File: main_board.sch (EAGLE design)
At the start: 49 parts, among them IC1 LT1168ACS8, IC2 LT1168ACS8, IC3 LT1168ACS8, IC4 317EMP, U1 TLC272IP, U2 TLC272IP, U3 TLC272IP

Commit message: Progress
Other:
- moved on the sheet: R2
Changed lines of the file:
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@@
 <instance part="SUPPLY10" gate="GND" x="182.88" y="15.24"/>
 <instance part="VDD1" gate="G$1" x="88.9" y="55.88"/>
-<instance part="R2" gate="G$1" x="88.9" y="45.72" rot="R90"/>
+<instance part="R2" gate="G$1" x="88.9" y="48.26" rot="R90"/>
 <instance part="R3" gate="G$1" x="78.74" y="7.62"/>
 <instance part="R10" gate="G$1" x="170.18" y="30.48" rot="R90"/>
@@
 <pinref part="VDD1" gate="G$1" pin="VDD"/>
 <pinref part="R2" gate="G$1" pin="2"/>
-<wire x1="88.9" y1="53.34" x2="88.9" y2="50.8" width="0.1524" layer="91"/>
 </segment>
 <segment>
@@
 <pinref part="R2" gate="G$1" pin="1"/>
 <pinref part="TM2" gate="G$1" pin="A"/>
-<wire x1="88.9" y1="40.64" x2="88.9" y2="38.1" width="0.1524" layer="91"/>
+<wire x1="88.9" y1="43.18" x2="88.9" y2="38.1" width="0.1524" layer="91"/>
 <wire x1="106.68" y1="38.1" x2="88.9" y2="38.1" width="0.1524" layer="91"/>
 <junction x="88.9" y="38.1"/>

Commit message: Merging
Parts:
- removed PAD1, PAD10, PAD11, PAD12, PAD2, PAD25, PAD26, PAD27, PAD28, PAD29, PAD3, PAD30, PAD4, PAD5, PAD6, PAD7, PAD8, PAD9: (no value), wirepad:1,6/0,9
- added C3, C4, C5, C6, C7: 10uF, adafruit:C-USC2012
- added X1, X2, X3: C-GRID-04-70543, con-molex:C-GRID-04-70543
- added X4, X5, X6: C-GRID-02-70543, con-molex:C-GRID-02-70543
- C1: value (none) -> 1uF; device eagle-ltspice:CC2012 -> adafruit:C-USC2012
- C2: value (none) -> 10uF; device eagle-ltspice:CC2012 -> adafruit:C-USC2012
- R13, R7: value (none) -> 30kO
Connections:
- net N$11 renamed U3_1_IN+
- net N$12 renamed IC3_RG1
- net N$13 renamed TM7POT2
- net N$14 renamed IC3_RG8
- net N$15 renamed U3_2_IN+
- net N$2 renamed U1_2IN-
- net N$20 renamed U1_2IN+
- net N$24 renamed U2_2IN-
- net N$25 renamed U2_1IN+
- net N$26 renamed U2_1IN-
- net N$27 renamed TM5POT2
- net N$3 renamed U1_1IN+
- net N$30 renamed U2_2IN+
- net N$4 renamed U1_1IN-
- net N$5 renamed TM2POT2
- net N$6 renamed ADJ
- net N$8 renamed U3_2_IN-
- net N$9 renamed U3_1_IN-
- removed net N$17: IC3.+IN, PAD2.P
- removed net N$18: IC3.-IN, PAD1.P
- removed net N$21: IC1.+IN, PAD26.P
- removed net N$22: IC1.-IN, PAD25.P
- removed net N$31: IC2.+IN, PAD29.P
- removed net N$32: IC2.-IN, PAD28.P
- new net BLUE_IN_B: IC3.+IN, X1-2.S
- new net BLUE_IN_R: IC3.-IN, X1-3.S
- new net GREEN_IN_B: IC1.+IN, X2-2.S
- new net GREEN_IN_R: IC1.-IN, X2-3.S
- new net WHITE_IN_B: IC2.+IN, X3-2.S
- new net WHITE_IN_R: IC2.-IN, X3-3.S
- net GND: now also C3.2, C4.1, C5.1, C6.1, C7.2, X1-4.S, X2-4.S, X3-4.S, X4-2.S, X5-2.S, X6-2.S; no longer PAD10.P, PAD11.P, PAD12.P, PAD7.P, PAD8.P, PAD9.P
- net N$1: now also X4-1.S; no longer PAD27.P
- net N$23: now also X5-1.S; no longer PAD30.P
- net N$7: no longer PAD3.P
- net VCC: now also C4.2, C5.2, C6.2
- net VDD: now also C3.1, C7.1, X1-1.S, X2-1.S, X3-1.S; no longer PAD4.P, PAD5.P, PAD6.P
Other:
- note added: "1. Assign values to all capacitors/resistors, etc... 2. Replace pin headers with MOLEX headers 3. Add capacitor to each output VDD 4. Name your NETS!"
- note removed: "Blue +"
- note removed: "Blue -"
- note removed: "Blue out_B"
- note removed: "Blue out_R"
- note removed: "Green +"
- note removed: "Green -"
- note removed: "Green out_B"
- note removed: "Green out_R"
- note removed: "TransducerGND"
- note removed: "TransducerVDD"
- note removed: "white -"
- note removed: "white+"
- note removed: "white-"
- moved on the sheet: C2, R9

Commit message: Finished board
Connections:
- net N$1 renamed U1_2OUT
- net N$23 renamed U2_2OUT
- net N$7 renamed U3_2OUT
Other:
- moved on the sheet: R12, R2
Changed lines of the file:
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@@
 <instance part="SUPPLY10" gate="GND" x="182.88" y="15.24"/>
 <instance part="VDD1" gate="G$1" x="88.9" y="55.88"/>
-<instance part="R2" gate="G$1" x="88.9" y="48.26" rot="R90"/>
+<instance part="R2" gate="G$1" x="88.9" y="50.8" rot="R90"/>
 <instance part="R3" gate="G$1" x="78.74" y="7.62"/>
 <instance part="R10" gate="G$1" x="170.18" y="30.48" rot="R90"/>
@@
 <instance part="SUPPLY14" gate="GND" x="182.88" y="71.12"/>
 <instance part="VDD2" gate="G$1" x="88.9" y="111.76"/>
-<instance part="R12" gate="G$1" x="88.9" y="101.6" rot="R90"/>
+<instance part="R12" gate="G$1" x="88.9" y="104.14" rot="R90"/>
 <instance part="R13" gate="G$1" x="78.74" y="63.5"/>
 <instance part="R14" gate="G$1" x="170.18" y="86.36" rot="R90"/>
@@
 </segment>
 </net>
-<net name="N$7" class="0">
+<net name="U3_2OUT" class="0">
 <segment>
 <pinref part="R4" gate="G$1" pin="2"/>
@@
 <pinref part="VDD1" gate="G$1" pin="VDD"/>
 <pinref part="R2" gate="G$1" pin="2"/>
+<wire x1="88.9" y1="55.88" x2="88.9" y2="53.34" width="0.1524" layer="91"/>
 </segment>
 <segment>
 <pinref part="VDD2" gate="G$1" pin="VDD"/>
 <pinref part="R12" gate="G$1" pin="2"/>
-<wire x1="88.9" y1="109.22" x2="88.9" y2="106.68" width="0.1524" layer="91"/>
 </segment>
 <segment>
@@
 </segment>
 </net>
-<net name="N$1" class="0">
+<net name="U1_2OUT" class="0">
 <segment>
 <pinref part="R1" gate="G$1" pin="2"/>
@@
 <pinref part="R2" gate="G$1" pin="1"/>
 <pinref part="TM2" gate="G$1" pin="A"/>
-<wire x1="88.9" y1="43.18" x2="88.9" y2="38.1" width="0.1524" layer="91"/>
+<wire x1="88.9" y1="45.72" x2="88.9" y2="38.1" width="0.1524" layer="91"/>
 <wire x1="106.68" y1="38.1" x2="88.9" y2="38.1" width="0.1524" layer="91"/>
 <junction x="88.9" y="38.1"/>
@@
 </segment>
 </net>
-<net name="N$23" class="0">
+<net name="U2_2OUT" class="0">
 <segment>
 <pinref part="R11" gate="G$1" pin="2"/>
@@
 <pinref part="R12" gate="G$1" pin="1"/>
 <pinref part="TM4" gate="G$1" pin="A"/>
-<wire x1="88.9" y1="96.52" x2="88.9" y2="93.98" width="0.1524" layer="91"/>
+<wire x1="88.9" y1="99.06" x2="88.9" y2="93.98" width="0.1524" layer="91"/>
 <wire x1="106.68" y1="93.98" x2="88.9" y2="93.98" width="0.1524" layer="91"/>
 <junction x="88.9" y="93.98"/>

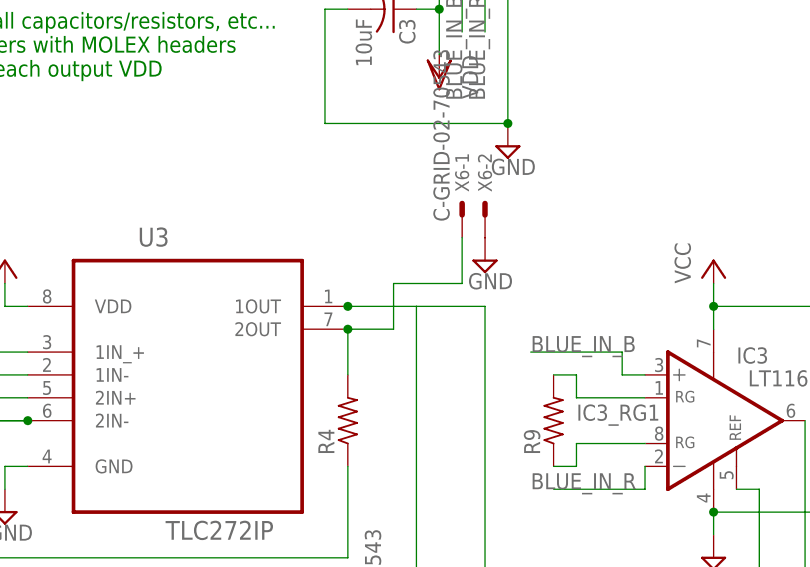
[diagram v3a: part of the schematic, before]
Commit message: Finished board. No errors remaining.
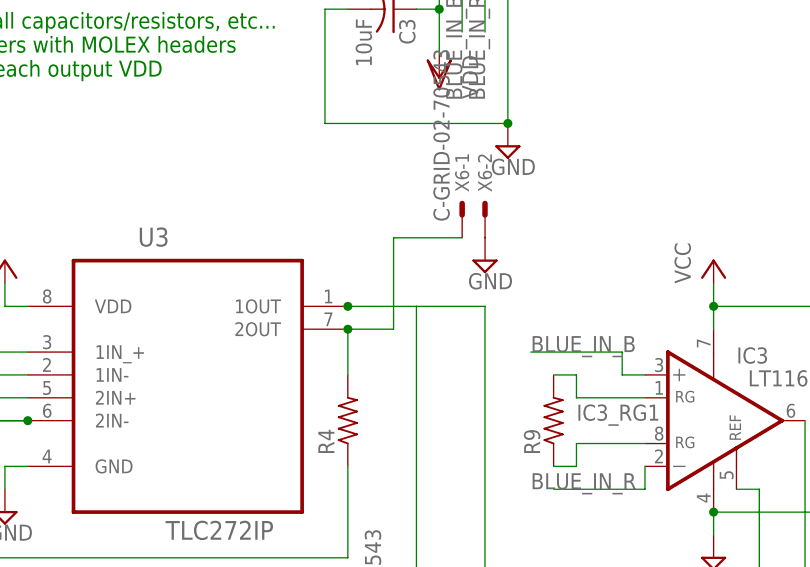
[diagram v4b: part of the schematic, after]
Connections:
- net U3_2OUT: now also X6-1.S
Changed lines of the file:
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@@
 </variantdefs>
 <classes>
-<class number="0" name="default" width="0.3048" drill="0.508">
+<class number="0" name="default" width="0.3048" drill="0.4318">
 <clearance class="0" value="0.254"/>
 </class>
@@
 <pinref part="U3" gate="A" pin="2OUT"/>
 <wire x1="142.24" y1="144.78" x2="142.24" y2="149.86" width="0.1524" layer="91"/>
-<wire x1="142.24" y1="149.86" x2="147.32" y2="149.86" width="0.1524" layer="91"/>
+<pinref part="X6" gate="-1" pin="S"/>
+<wire x1="154.94" y1="160.02" x2="147.32" y2="160.02" width="0.1524" layer="91"/>
+<wire x1="147.32" y1="160.02" x2="147.32" y2="149.86" width="0.1524" layer="91"/>
+<wire x1="147.32" y1="149.86" x2="142.24" y2="149.86" width="0.1524" layer="91"/>
 <junction x="142.24" y="149.86"/>
-<wire x1="147.32" y1="149.86" x2="147.32" y2="154.94" width="0.1524" layer="91"/>
-<wire x1="147.32" y1="154.94" x2="154.94" y2="154.94" width="0.1524" layer="91"/>
-<wire x1="154.94" y1="154.94" x2="154.94" y2="160.02" width="0.1524" layer="91"/>
 </segment>
 </net>

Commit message: Finished.
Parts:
- R1, R4: value (none) -> 10kO
- R10: value (none) -> 110ohm
- R11: value (none) -> 10kO\
- R12, R2: value (none) -> 30kO
- R13: value 30kO -> 2kO
- R14, R9: value (none) -> 110 ohm
- R3, R8: value (none) -> 2kO
- R5: value (none) -> 1KO
- R6: value (none) -> 4kO
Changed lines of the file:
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@@
 <parts>
 <part name="IC3" library="linear-technology" library_urn="urn:adsk.eagle:library:261" deviceset="LT1168" device="S8" technology="AC"/>
-<part name="R4" library="adafruit" deviceset="R-US_" device="R1206"/>
-<part name="R5" library="adafruit" deviceset="R-US_" device="R1206"/>
-<part name="R6" library="adafruit" deviceset="R-US_" device="R1206"/>
+<part name="R4" library="adafruit" deviceset="R-US_" device="R1206" value="10kO"/>
+<part name="R5" library="adafruit" deviceset="R-US_" device="R1206" value="1KO"/>
+<part name="R6" library="adafruit" deviceset="R-US_" device="R1206" value="4kO"/>
 <part name="U3" library="Texas Instruments_By_element14_Batch_1" deviceset="TLC272IP" device=""/>
 <part name="SUPPLY3" library="supply2" library_urn="urn:adsk.eagle:library:372" deviceset="GND" device=""/>
@@
 <part name="TM6" library="adafruit" deviceset="TRIMPOT" device="3386"/>
 <part name="TM7" library="adafruit" deviceset="TRIMPOT" device="3386"/>
-<part name="G1" library="battery" library_urn="urn:adsk.eagle:library:109" deviceset="AB9V" device=""/>
 <part name="P+4" library="supply1" library_urn="urn:adsk.eagle:library:371" deviceset="VCC" device=""/>
 <part name="P+8" library="supply1" library_urn="urn:adsk.eagle:library:371" deviceset="VCC" device=""/>
@@
 <part name="VDD4" library="supply1" library_urn="urn:adsk.eagle:library:371" deviceset="VDD" device=""/>
 <part name="R7" library="adafruit" deviceset="R-US_" device="R1206" value="30kO"/>
-<part name="R8" library="adafruit" deviceset="R-US_" device="R1206"/>
-<part name="R9" library="adafruit" deviceset="R-US_" device="R1206"/>
+<part name="R8" library="adafruit" deviceset="R-US_" device="R1206" value="2kO"/>
+<part name="R9" library="adafruit" deviceset="R-US_" device="R1206" value="110 ohm"/>
 <part name="P+1" library="supply1" library_urn="urn:adsk.eagle:library:371" deviceset="VCC" device=""/>
 <part name="P+2" library="supply1" library_urn="urn:adsk.eagle:library:371" deviceset="VCC" device=""/>
 <part name="IC1" library="linear-technology" library_urn="urn:adsk.eagle:library:261" deviceset="LT1168" device="S8" technology="AC"/>
-<part name="R1" library="adafruit" deviceset="R-US_" device="R1206"/>
+<part name="R1" library="adafruit" deviceset="R-US_" device="R1206" value="10kO"/>
 <part name="U1" library="Texas Instruments_By_element14_Batch_1" deviceset="TLC272IP" device=""/>
 <part name="SUPPLY1" library="supply2" library_urn="urn:adsk.eagle:library:372" deviceset="GND" device=""/>
@@
 <part name="SUPPLY10" library="supply2" library_urn="urn:adsk.eagle:library:372" deviceset="GND" device=""/>
 <part name="VDD1" library="supply1" library_urn="urn:adsk.eagle:library:371" deviceset="VDD" device=""/>
-<part name="R2" library="adafruit" deviceset="R-US_" device="R1206"/>
-<part name="R3" library="adafruit" deviceset="R-US_" device="R1206"/>
-<part name="R10" library="adafruit" deviceset="R-US_" device="R1206"/>
+<part name="R2" library="adafruit" deviceset="R-US_" device="R1206" value="30kO"/>
+<part name="R3" library="adafruit" deviceset="R-US_" device="R1206" value="2kO"/>
+<part name="R10" library="adafruit" deviceset="R-US_" device="R1206" value="110ohm"/>
 <part name="P+3" library="supply1" library_urn="urn:adsk.eagle:library:371" deviceset="VCC" device=""/>
 <part name="P+5" library="supply1" library_urn="urn:adsk.eagle:library:371" deviceset="VCC" device=""/>
 <part name="IC2" library="linear-technology" library_urn="urn:adsk.eagle:library:261" deviceset="LT1168" device="S8" technology="AC"/>
-<part name="R11" library="adafruit" deviceset="R-US_" device="R1206"/>
+<part name="R11" library="adafruit" deviceset="R-US_" device="R1206" value="10kO\"/>
 <part name="U2" library="Texas Instruments_By_element14_Batch_1" deviceset="TLC272IP" device=""/>
 <part name="SUPPLY11" library="supply2" library_urn="urn:adsk.eagle:library:372" deviceset="GND" device=""/>
@@
 <part name="SUPPLY14" library="supply2" library_urn="urn:adsk.eagle:library:372" deviceset="GND" device=""/>
 <part name="VDD2" library="supply1" library_urn="urn:adsk.eagle:library:371" deviceset="VDD" device=""/>
-<part name="R12" library="adafruit" deviceset="R-US_" device="R1206"/>
-<part name="R13" library="adafruit" deviceset="R-US_" device="R1206" value="30kO"/>
-<part name="R14" library="adafruit" deviceset="R-US_" device="R1206"/>
+<part name="R12" library="adafruit" deviceset="R-US_" device="R1206" value="30kO"/>
+<part name="R13" library="adafruit" deviceset="R-US_" device="R1206" value="2kO"/>
+<part name="R14" library="adafruit" deviceset="R-US_" device="R1206" value="110 ohm"/>
 <part name="P+6" library="supply1" library_urn="urn:adsk.eagle:library:371" deviceset="VCC" device=""/>
 <part name="P+7" library="supply1" library_urn="urn:adsk.eagle:library:371" deviceset="VCC" device=""/>
@@
 <part name="SUPPLY16" library="supply2" library_urn="urn:adsk.eagle:library:372" deviceset="GND" device=""/>
 <part name="SUPPLY22" library="supply2" library_urn="urn:adsk.eagle:library:372" deviceset="GND" device=""/>
+<part name="G1" library="battery" deviceset="AB9V" device=""/>
 </parts>
 <sheets>
@@
 <instance part="TM6" gate="G$1" x="83.82" y="147.32" rot="MR270"/>
 <instance part="TM7" gate="G$1" x="83.82" y="124.46" rot="R270"/>
-<instance part="G1" gate="G$1" x="40.64" y="152.4"/>
 <instance part="P+4" gate="VCC" x="58.42" y="157.48"/>
 <instance part="P+8" gate="VCC" x="27.94" y="132.08"/>
@@
 <instance part="SUPPLY16" gate="GND" x="152.4" y="104.14"/>
 <instance part="SUPPLY22" gate="GND" x="152.4" y="48.26"/>
+<instance part="G1" gate="G$1" x="40.64" y="152.4"/>
 </instances>
 <busses>
@@
 </segment>
 <segment>
-<pinref part="G1" gate="G$1" pin="-"/>
 <pinref part="SUPPLY4" gate="GND" pin="GND"/>
 <wire x1="27.94" y1="152.4" x2="22.86" y2="152.4" width="0.1524" layer="91"/>
@@
 <wire x1="38.1" y1="142.24" x2="27.94" y2="142.24" width="0.1524" layer="91"/>
 <wire x1="27.94" y1="142.24" x2="27.94" y2="152.4" width="0.1524" layer="91"/>
+<pinref part="C1" gate="G$1" pin="2"/>
+<pinref part="G1" gate="G$1" pin="-"/>
 <junction x="27.94" y="152.4"/>
-<pinref part="C1" gate="G$1" pin="2"/>
 </segment>
 <segment>
@@
 <net name="VCC" class="0">
 <segment>
-<pinref part="G1" gate="G$1" pin="+"/>
 <pinref part="P+4" gate="VCC" pin="VCC"/>
 <wire x1="53.34" y1="152.4" x2="58.42" y2="152.4" width="0.1524" layer="91"/>
@@
 <wire x1="45.72" y1="142.24" x2="53.34" y2="142.24" width="0.1524" layer="91"/>
 <wire x1="53.34" y1="142.24" x2="53.34" y2="152.4" width="0.1524" layer="91"/>
+<pinref part="C1" gate="G$1" pin="1"/>
+<pinref part="G1" gate="G$1" pin="+"/>
 <junction x="53.34" y="152.4"/>
-<pinref part="C1" gate="G$1" pin="1"/>
-</segment>
-<segment>
+</segment>
+<segment>
